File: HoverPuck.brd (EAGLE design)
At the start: 50 x 20 mm, 47 parts, among them J2 1X4, U1 EFM8BB1.QFN20, U2 TPS62177.DQC, U3 LM2731.DBV, U4 BLE112-A

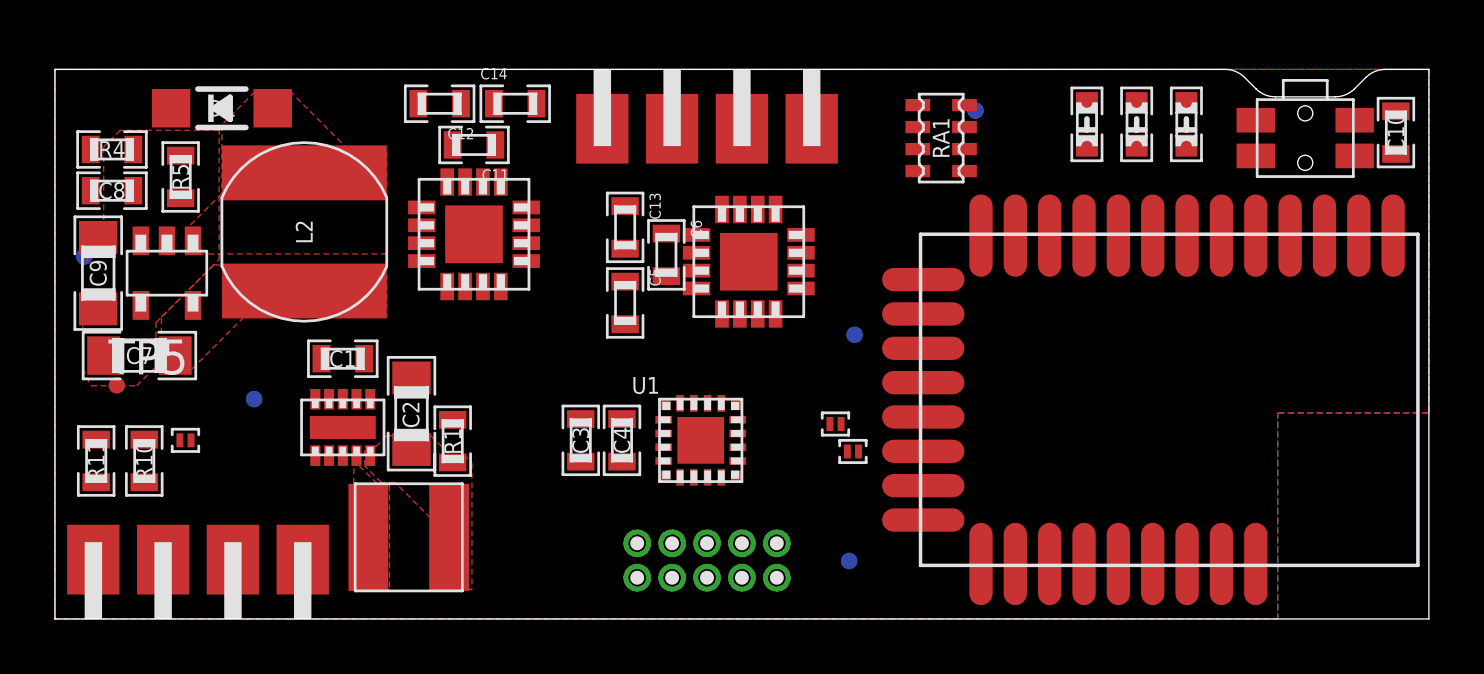
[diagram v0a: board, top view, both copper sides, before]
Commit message: Working on v1.1 Schematic almost complete, need to work on routing pins now. Decided to not be stingy and control the full H Brudge with two sets of PWMs instead of one. I have the pins, might as well.
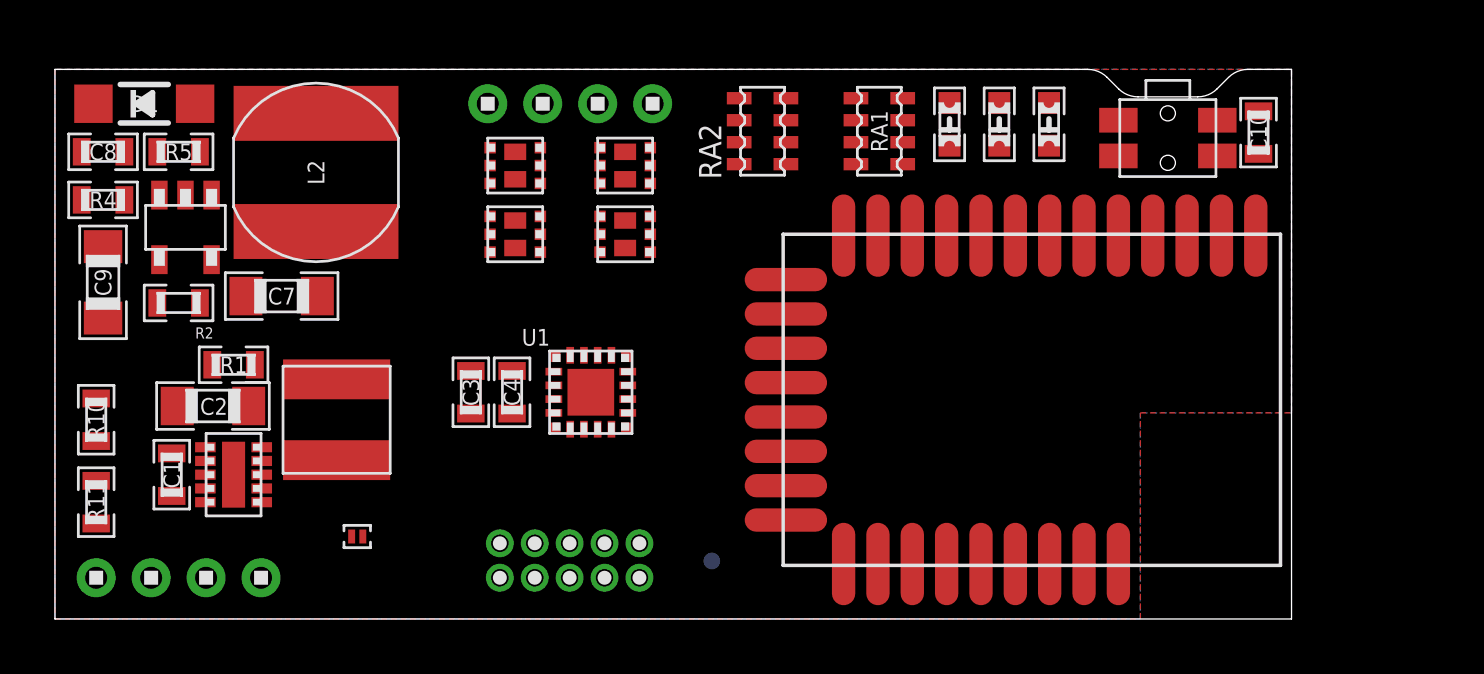
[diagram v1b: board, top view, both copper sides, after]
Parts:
- removed C11, C12, C13, C14, C5, C6: 0.1uF, standardparts:0603
- removed J6, J7: (no value), solderjumper:2.SML.PASTE
- removed MB0, MB1: 1X2, headers.edge(.1in):1X2
- removed TP3, TP4, TP5, TP6: TPTP06R, testpad:TP06R
- removed U5, U6: (no value), packages(ti):RTY.16
- added Q1, Q2, Q3, Q4: (no value), fairchild:MICROFET.2X2
- added R2: 51k, standardparts:0603
- added RA2: 1k, resistorarray:0603.4.C
- added SJ1: (no value), solderjumper:2.SML.PASTE
- J1: value (none) -> 1X4; device solderjumper:2.SML.PASTE -> headers(2mm):1X4
- J2: device headers.edge(.1in):1X4 -> headers(2mm):1X4
- RA1: value (none) -> 1k
- moved J2 21.1 mm to (18.8, 18.8), turned to 0 degrees
- moved R1 8.45 mm to (6.50, 9.25), turned to 0 degrees
- moved C1 7.52 mm to (4.25, 5.25), turned to 270 degrees
- moved C2 7.23 mm to (5.75, 7.75), turned to 180 degrees
- moved C7 5.61 mm to (8.25, 11.8), turned to 0 degrees
- moved TP2 5.50 mm to (1.06, 18.7)
- moved L1 5.02 mm to (10.2, 7.25), turned to 90 degrees
- moved J1 5.01 mm to (4.50, 1.50), turned to 180 degrees
- moved B1 5.00 mm to (40.5, 17.5)
- moved C10 5.00 mm to (43.8, 17.7)
- moved D2 5.00 mm to (32.6, 18.0)
- moved D3 5.00 mm to (34.4, 18.0)
- moved D4 5.00 mm to (36.2, 18.0)
- moved TP1 5.00 mm to (23.9, 2.11)
- moved U$38 5.00 mm to (21.3, 2.75)
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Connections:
- removed net 12V: C12.1, C13.1, C14.1, C5.1, U5.8, U6.8
- removed net 20V_EN: RA1.4, TP5.TP, U1.2, U3.4
- removed net N$10: J6.1, U4.24
- removed net N$11: J7.1, U4.23
- removed net N$14: MB0.2, U5.9
- removed net N$15: MB1.1, U6.6
- removed net N$16: MB1.2, U6.9
- removed net N$17: C6.1, U5.10
- removed net N$18: C6.2, U5.11
- removed net N$19: C11.2, U6.11
- removed net N$20: C11.1, U6.10
- new net MB0+: J2.1, Q1.1, Q2.3, Q2.PAD@2
- new net MB0-: J2.2, Q1.4, Q2.6, Q2.PAD@1
- new net MB1+: J2.3, Q3.1, Q4.3, Q4.PAD@2
- new net MB1-: J2.4, Q3.4, Q4.6, Q4.PAD@1
- new net PWM0+: Q1.2, Q2.2, RA2.4
- new net PWM0-: Q1.5, Q2.5, RA2.2
- new net PWM1+: Q3.2, Q4.2, RA2.8
- new net PWM1-: Q3.5, Q4.5, RA2.6
- net 1S_DBG: now also J1.3; no longer J2.3
- net 20V: now also Q1.3, Q1.6, Q1.PAD@1, Q1.PAD@2, Q3.3, Q3.6, Q3.PAD@1, Q3.PAD@2
- net 3.3V: no longer U5.16, U5.4, U6.16, U6.4
- net ADC0: now also SJ1.2; no longer J1.2
- net EN_20V: now also R2.2, RA1.4, U1.2, U3.4; no longer U5.3, U6.3
- net GND: now also J1.4, Q2.1, Q2.4, Q4.1, Q4.4, RA2.1, RA2.3, RA2.5, RA2.7, U4.26; no longer C13.2, C14.2, J2.4, TP6.TP, U5.12, U5.2, U5.7, U5.PAD, U6.12, U6.2, U6.7, U6.PAD
- net N$1: now also U1.13; no longer C12.2, U6.13
- net N$12: now also SJ1.1; no longer J1.1
- net N$13: now also U1.10; no longer MB0.1, U5.6
- net N$2: now also U1.11; no longer C5.2, U5.13
- net PWM0: no longer TP3.TP, U5.1
- net PWM1: no longer TP4.TP, U6.1
- net RXI: now also U4.24; no longer J6.2
- net TXO: now also U4.23; no longer J7.2
- net VBAT: now also J1.1, R2.1; no longer J2.1
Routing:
- removed copper zone on layer 1, net 3.3V
- removed copper zone on layer 1, net N$3
- removed copper zone on layer 1, net N$5
- removed copper zone on layer 1, net VBAT
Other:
- board size 50 x 20 mm -> 45 x 20 mm
- board text removed: "20v"
- board text removed: "3.3v"
- board text removed: "PWM0"
- board text removed: "PWM1"

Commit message: HoverPuck v1.1 completed. Send to OSHPark and PCBWay
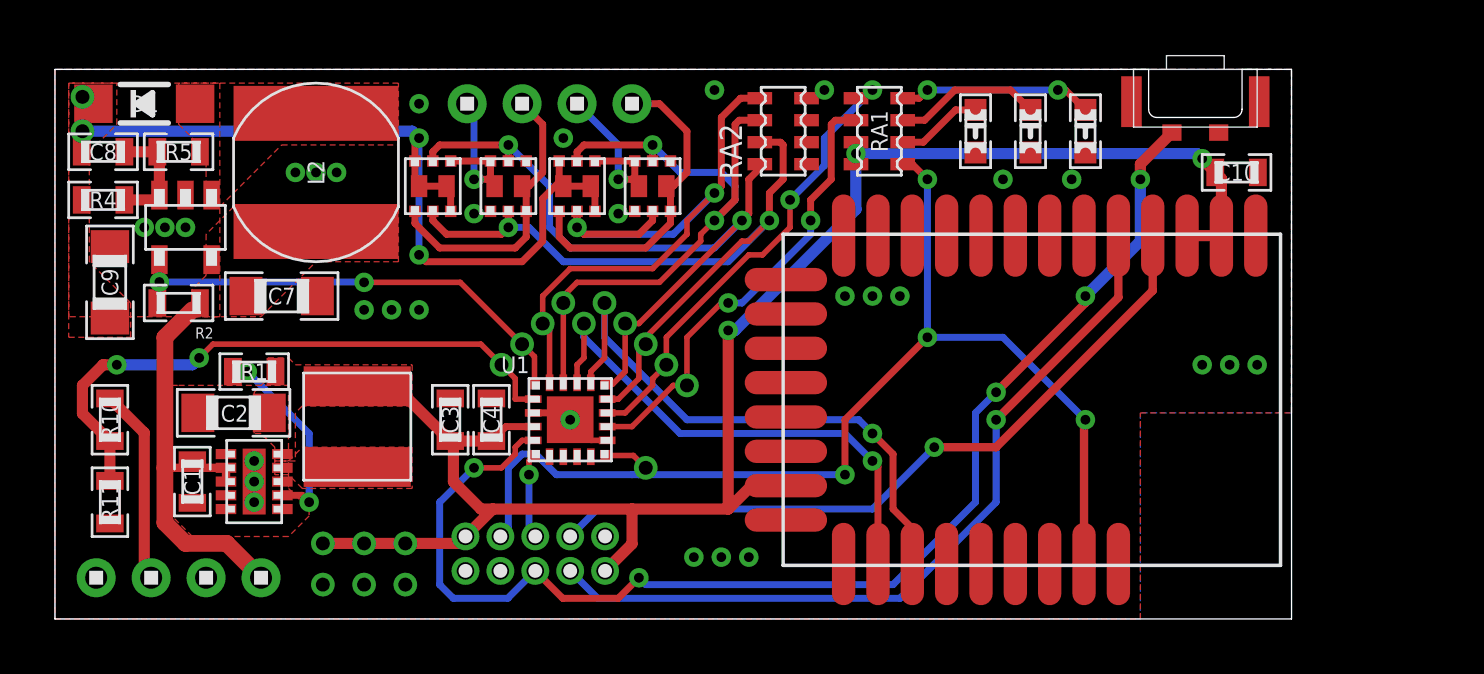
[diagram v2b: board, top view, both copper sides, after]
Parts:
- removed B1: (no value), alps:SKSCLDE010
- removed SJ1: (no value), solderjumper:2.SML.PASTE
- removed TP1, TP2: TPTP06R, testpad:TP06R
- added S1: SKSLLAE010, alps:SKSLLAE010
- moved Q1 3.47 mm to (13.8, 15.8), turned to 180 degrees
- moved Q3 2.47 mm to (19.0, 15.8), turned to 180 degrees
- moved C10 1.66 mm to (43.0, 16.2), turned to 0 degrees
- moved D4 1.35 mm to (37.5, 17.8), turned to 270 degrees
- moved U$38 1.27 mm to (20.0, 3.00)
- moved U$39 1.27 mm to (20.0, 1.75)
- moved C4 1.25 mm to (15.9, 7.25)
- moved C3 1.25 mm to (14.4, 7.25)
- moved Q4 1.25 mm to (21.8, 15.8), turned to 180 degrees
- moved U1 1.25 mm to (18.8, 7.25)
- moved D3 1.16 mm to (35.5, 17.8), turned to 270 degrees
- moved D2 0.98 mm to (33.5, 17.8), turned to 270 degrees
- moved C1 0.79 mm to (5.00, 5.00)
- moved C2 0.79 mm to (6.50, 7.50)
- moved L1 0.79 mm to (11.0, 7.00)
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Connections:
- removed net N$1: U1.13
- removed net N$12: SJ1.1, U1.1
- removed net N$13: U1.10
- removed net N$2: U1.11
- removed net PWM0: U1.19
- removed net PWM1: U1.16
- removed net STATUS: RA1.2, U1.15
- new net STAT1: RA1.3, U1.13
- new net STAT2: RA1.1, U1.14
- net 20V: no longer TP2.TP
- net 3.3V: now also RA1.5, RA1.7; no longer RA1.6, RA1.8, TP1.TP
- net ADC0: now also U1.2; no longer SJ1.2
- net BLE_!RST: now also RA1.8, U1.11; no longer RA1.5, U1.14
- net EFM8_C2CK: now also S1.1; no longer B1.3, B1.4
- net EN_20V: now also U1.1; no longer RA1.4, U1.2
- net GND: now also S1.2; no longer B1.1, B1.2
- net N$4: now also RA1.6; no longer RA1.7
- net N$8: now also D3.P$1, RA1.4; no longer D4.P$1, RA1.1
- net N$9: now also D4.P$1, RA1.2; no longer D3.P$1, RA1.3
- net PWM0+: now also RA2.2, U1.16; no longer RA2.4
- net PWM0-: now also RA2.4, U1.15; no longer RA2.2
- net PWM1+: now also RA2.6, U1.19; no longer RA2.8
- net PWM1-: now also RA2.8, U1.20; no longer RA2.6
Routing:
- net 3.3V: track 0.00 -> 65.8 mm, vias 0 -> 6
- net EFM8_C2CK: track 0.00 -> 46.1 mm, vias 0 -> 5
- net BLE_!RST: track 0.00 -> 42.8 mm, vias 0 -> 5
- net 20V: track 0.00 -> 31.5 mm, vias 0 -> 4
- net BLE_DD: track 0.00 -> 28.9 mm, vias 0 -> 1
- net PWM0-: track 0.00 -> 28.1 mm, vias 0 -> 3
- net BLE_DC: track 0.00 -> 26.9 mm, vias 0 -> 1
- net PWM0+: track 0.00 -> 26.0 mm, vias 0 -> 3
- net PWM1-: track 0.00 -> 25.9 mm, vias 0 -> 3
- net PWM1+: track 0.00 -> 23.8 mm, vias 0 -> 3
- net ADC0: track 0.00 -> 22.2 mm, vias 0 -> 3
- net RXI: track 0.00 -> 20.9 mm, vias 0 -> 2
- net TXO: track 0.00 -> 19.0 mm, vias 0 -> 2
- net EN_20V: track 0.00 -> 17.4 mm, vias 0 -> 3
- net STAT2: track 0.00 -> 17.2 mm, vias 0 -> 3
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- added copper zone on layer 1, net 20V
- added copper zone on layer 1, net 3.3V
- added copper zone on layer 1, net N$3
- added copper zone on layer 1, net N$5
- added copper zone on layer 1, net VBAT
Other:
- outline, holes or cut-outs redrawn
- board text added: "20V"
- board text added: "3.3V"
- board text added: "BLE_!RST"
- board text added: "EN_20V"
- board text added: "PWM0+"
- board text added: "PWM0-"
- board text added: "PWM1+"
- board text added: "PWM1-"
- board text added: "RXI"
- board text added: "STAT1"
- board text added: "STAT2"
- board text added: "TXO"
- board text added: "VBAT (1S)/2"
